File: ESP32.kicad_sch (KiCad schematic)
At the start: 20 parts, among them J1 USB_B_Micro, SW1 Boot, SW2 Reset, U3 ESP32-S3-MINI-1, U4 USBLC6-2SC6

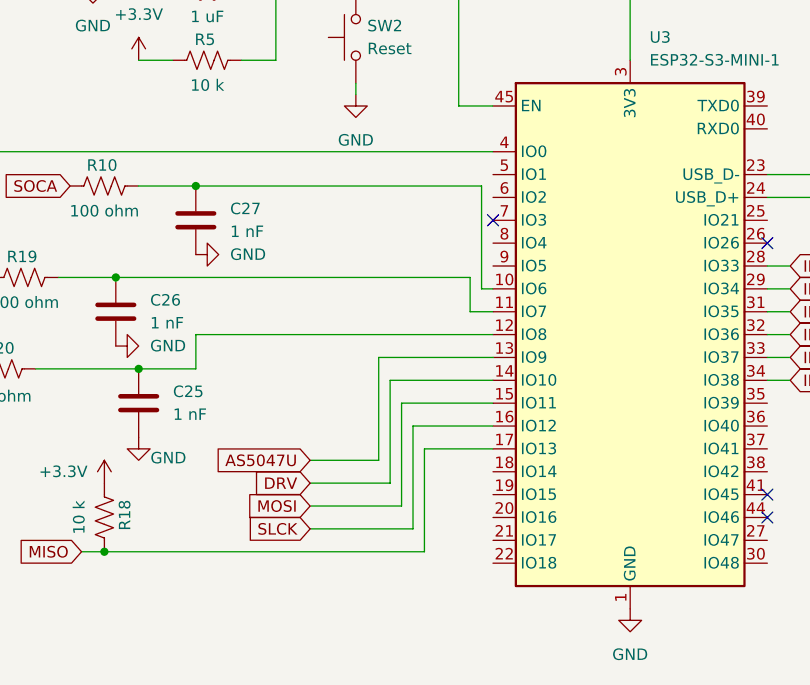
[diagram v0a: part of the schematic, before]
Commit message: Added additional Labels
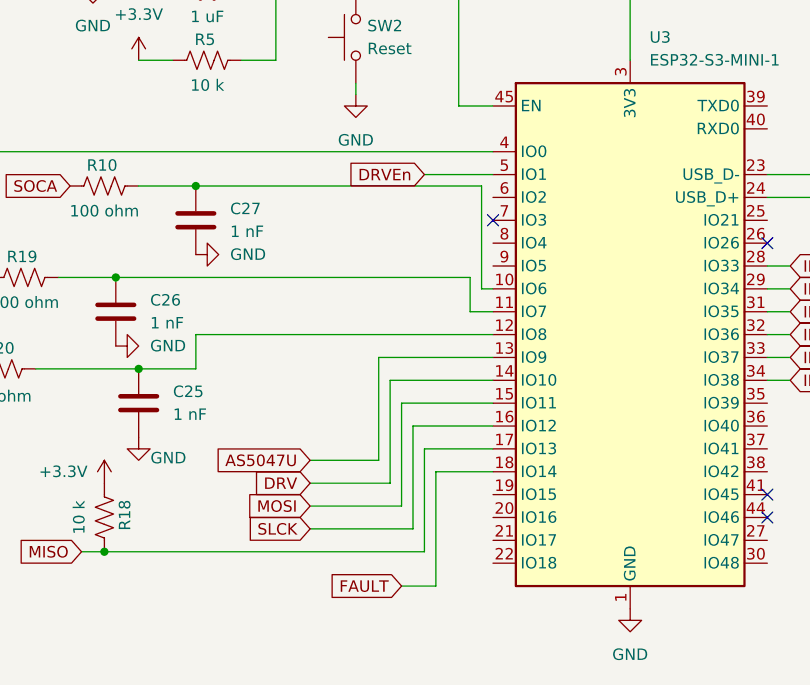
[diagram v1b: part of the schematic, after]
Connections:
- net FAULT: now reaches U3.18 (IO14)
- net DRVEn: now reaches U3.5 (IO1)
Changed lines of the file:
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@@
+	(wire
+		(pts
+			(xy 123.19 78.74) (xy 130.81 78.74)
+		)
+		(stroke
+			(width 0)
+			(type default)
+		)
+	)
 	(wire
 		(pts
@@
 	(wire
 		(pts
+			(xy 124.46 124.46) (xy 124.46 111.76)
+		)
+		(stroke
+			(width 0)
+			(type default)
+		)
+	)
+	(wire
+		(pts
 			(xy 118.11 110.49) (xy 118.11 99.06)
 		)
@@
 	(wire
 		(pts
+			(xy 124.46 111.76) (xy 130.81 111.76)
+		)
+		(stroke
+			(width 0)
+			(type default)
+		)
+	)
+	(wire
+		(pts
 			(xy 161.29 78.74) (xy 212.09 78.74)
 		)
@@
 	(wire
 		(pts
+			(xy 120.65 124.46) (xy 124.46 124.46)
+		)
+		(stroke
+			(width 0)
+			(type default)
+		)
+	)
+	(wire
+		(pts
 			(xy 106.68 57.15) (xy 106.68 58.42)
 		)
@@
 		)
 	)
+	(global_label "DRVEn"
+		(shape input)
+		(at 123.19 78.74 180)
+		(fields_autoplaced yes)
+		(effects
+			(font
+				(size 1.27 1.27)
+			)
+			(justify right)
+		)
+		(property "Intersheetrefs" "${INTERSHEET_REFS}"
+			(at 114.2782 78.74 0)
+			(effects
+				(font
+					(size 1.27 1.27)
+				)
+				(justify right)
+				(hide yes)
+			)
+		)
+	)
 	(global_label "MOSI"
 		(shape input)
@@
 			(effects
 				(font
+					(size 1.27 1.27)
+				)
+				(justify right)
+				(hide yes)
+			)
+		)
+	)
+	(global_label "FAULT"
+		(shape input)
+		(at 120.65 124.46 180)
+		(fields_autoplaced yes)
+		(effects
+			(font
+				(size 1.27 1.27)
+			)
+			(justify right)
+		)
+		(property "Intersheetrefs" "${INTERSHEET_REFS}"
+			(at 112.1614 124.46 0)
+			(effects
+				(font

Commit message: Layed out PCB
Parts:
- C10: footprint (none) -> Capacitor_SMD:C_0603_1608Metric
- C11, C24, C25, C26, C27, C8, C9: footprint (none) -> Capacitor_SMD:C_0402_1005Metric
- R10, R18, R19, R20, R5, R6: footprint (none) -> Resistor_SMD:R_0603_1608Metric
- SW1, SW2: footprint (none) -> SMD_Button:SW_3x6_SMD_LCSC
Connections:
- net SOCA: now also R20.1; no longer R10.1
- net SOCC: now also R10.1; no longer R20.1
- net D-: now reaches U3.23 (USB_D-), U4.4 (I/O2)
- net D-: now also J1.2 (D-), U4.3 (I/O2)
- net D+: now reaches U3.24 (USB_D+), U4.6 (I/O1)
- net D+: now also J1.3 (D+), U4.1 (I/O1)
- no-connect marks 5 -> 21
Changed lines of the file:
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@@
 	)
 	(no_connect
+		(at 161.29 121.92)
+	)
+	(no_connect
+		(at 130.81 121.92)
+	)
+	(no_connect
+		(at 130.81 81.28)
+	)
+	(no_connect
+		(at 130.81 116.84)
+	)
+	(no_connect
 		(at 161.29 116.84)
 	)
 	(no_connect
+		(at 130.81 86.36)
+	)
+	(no_connect
 		(at 161.29 86.36)
 	)
 	(no_connect
+		(at 161.29 71.12)
+	)
+	(no_connect
+		(at 161.29 109.22)
+	)
+	(no_connect
+		(at 130.81 88.9)
+	)
+	(no_connect
 		(at 233.68 76.2)
 	)
 	(no_connect
+		(at 161.29 73.66)
+	)
+	(no_connect
+		(at 161.29 106.68)
+	)
+	(no_connect
 		(at 130.81 83.82)
 	)
 	(no_connect
+		(at 161.29 83.82)
+	)
+	(no_connect
+		(at 161.29 119.38)
+	)
+	(no_connect
+		(at 130.81 114.3)
+	)
+	(no_connect
+		(at 161.29 104.14)
+	)
+	(no_connect
 		(at 161.29 114.3)
 	)
+	(no_connect
+		(at 130.81 119.38)
+	)
+	(no_connect
+		(at 161.29 111.76)
+	)
 	(wire
 		(pts
@@
 	(wire
 		(pts
+			(xy 109.22 85.09) (xy 109.22 80.01)
+		)
+		(stroke
+			(width 0)
+			(type default)
+		)
+	)
+	(wire
+		(pts
+			(xy 97.79 80.01) (xy 109.22 80.01)
+		)
+		(stroke
+			(width 0)
+			(type default)
+		)
+	)
+	(wire
+		(pts
 			(xy 161.29 96.52) (xy 163.83 96.52)
 		)
@@
 	(wire
 		(pts
+			(xy 129.54 85.09) (xy 109.22 85.09)
+		)
+		(stroke
+			(width 0)
+			(type default)
+		)
+	)
+	(wire
+		(pts
 			(xy 236.22 100.33) (xy 231.14 100.33)
 		)
@@
 	(wire
 		(pts
-			(xy 129.54 80.01) (xy 129.54 91.44)
-		)
-		(stroke
-			(width 0)
-			(type default)
-		)
-	)
-	(wire
-		(pts
 			(xy 63.5 76.2) (xy 130.81 76.2)
 		)
@@
 	(wire
 		(pts
-			(xy 97.79 80.01) (xy 129.54 80.01)
-		)
-		(stroke
-			(width 0)
-			(type default)
-		)
-	)
-	(wire
-		(pts
 			(xy 233.68 81.28) (xy 222.25 81.28)
 		)
@@
 	(wire
 		(pts
+			(xy 97.79 81.28) (xy 97.79 80.01)
+		)
+		(stroke
+			(width 0)
+			(type default)
+		)
+	)
+	(wire
+		(pts
 			(xy 214.63 90.17) (xy 217.17 90.17)
 		)
@@
 	(wire
 		(pts
+			(xy 129.54 91.44) (xy 129.54 85.09)
+		)
+		(stroke
+			(width 0)
+			(type default)
+		)
+	)
+	(wire
+		(pts
 			(xy 250.19 68.58) (xy 243.84 68.58)
 		)
@@
 		)
 	)
-	(global_label "SOCA"
-		(shape input)
-		(at 83.82 80.01 180)
-		(fields_autoplaced yes)
+	(label "D+"
+		(at 165.1 81.28 0)
 		(effects
 			(font
 				(size 1.27 1.27)
 			)
-			(justify right)
+			(justify left bottom)
 		)
-		(property "Intersheetrefs" "${INTERSHEET_REFS}"
-			(at 75.9362 80.01 0)
-			(effects
-				(font
-					(size 1.27 1.27)
-				)
-				(justify right)
-				(hide yes)
+	)
+	(label "D-"
+		(at 227.33 78.74 0)
+		(effects
+			(font
+				(size 1.27 1.27)
+			)
+			(justify left bottom)
+		)
+	)
+	(label "D+"
+		(at 227.33 81.28 0)
+		(effects
+			(font
+				(size 1.27 1.27)
+			)
+			(justify left bottom)
+		)
+	)
+	(label "D-"
+		(at 165.1 78.74 0)
+		(effects
+			(font
+				(size 1.27 1.27)
 			)
+			(justify left bottom)
 		)
 	)
@@
 		)
 	)
+	(global_label "SOCC"
+		(shape input)
+		(at 83.82 80.01 180)
+		(fields_autoplaced yes)
+		(effects
+			(font
+				(size 1.27 1.27)
+			)
+			(justify right)
+		)
+		(property "Intersheetrefs" "${INTERSHEET_REFS}"
+			(at 75.7548 80.01 0)
+			(effects
+				(font
+					(size 1.27 1.27)
+				)
+				(justify right)
+				(hide yes)
+			)
+		)
+	)
 	(global_label "SOCB"
 		(shape input)
@@
 		)
 	)
-	(global_label "MOSI"
+	(global_label "SOCA"
 		(shape input)
-		(at 110.49 115.57 180)
+		(at 71.12 100.33 180)
 		(fields_autoplaced yes)
 		(effects
@@
 		)
 		(property "Intersheetrefs" "${INTERSHEET_REFS}"
-			(at 102.9086 115.57 0)
+			(at 63.2362 100.33 0)
 			(effects
 				(font
@@
 		)
 	)
-	(global_label "AS5047U"
+	(global_label "MOSI"
 		(shape input)
-		(at 110.49 110.49 180)
+		(at 110.49 115.57 180)
 		(fields_autoplaced yes)
 		(effects
@@
 		)
 		(property "Intersheetrefs" "${INTERSHEET_REFS}"
-			(at 99.0382 110.49 0)
+			(at 102.9086 115.57 0)
 			(effects
 				(font
@@
 		)
 	)
-	(global_label "INLC"
+	(global_label "AS5047U"
 		(shape input)
-		(at 163.83 101.6 0)
+		(at 110.49 110.49 180)
 		(fields_autoplaced yes)
 		(effects
@@
 				(size 1.27 1.27)
 			)
-			(justify left)
+			(justify right)
 		)
 		(property "Intersheetrefs" "${INTERSHEET_REFS}"
-			(at 171.0486 101.6 0)
+			(at 99.0382 110.49 0)
 			(effects
 				(font
 					(size 1.27 1.27)
 				)
-				(justify left)
+				(justify right)
 				(hide yes)
 			)
 		)
 	)
-	(global_label "SOCC"
+	(global_label "INLC"
 		(shape input)
-		(at 71.12 100.33 180)
+		(at 163.83 101.6 0)
 		(fields_autoplaced yes)
 		(effects
@@
 				(size 1.27 1.27)
 			)
-			(justify right)
+			(justify left)
 		)
 		(property "Intersheetrefs" "${INTERSHEET_REFS}"
-			(at 63.0548 100.33 0)
+			(at 171.0486 101.6 0)
 			(effects
 				(font
 					(size 1.27 1.27)
 				)
-				(justify right)
+				(justify left)
 				(hide yes)
 			)
@@
 			)
 		)
-		(property "Footprint" ""
+		(property "Footprint" "Capacitor_SMD:C_0603_1608Metric"
 			(at 127.9652 50.8 0)
 			(effects
@@
 			)
 		)
-		(property "Footprint" ""
+		(property "Footprint" "Resistor_SMD:R_0603_1608Metric"
 			(at 88.646 117.094 90)
 			(effects
@@
 			)
 		)
-		(property "Footprint" ""
+		(property "Footprint" "Resistor_SMD:R_0603_1608Metric"
 			(at 78.994 89.154 90)
 			(effects
@@
 			)
 		)
-		(property "Footprint" ""
+		(property "Footprint" "Resistor_SMD:R_0603_1608Metric"
 			(at 87.884 78.994 90)
 			(effects
@@
 			)
 		)
-		(property "Footprint" ""
+		(property "Footprint" "Capacitor_SMD:C_0402_1005Metric"
 			(at 92.4052 107.95 0)
 			(effects
@@
 			)
 		)
-		(property "Footprint" ""
+		(property "Footprint" "Capacitor_SMD:C_0402_1005Metric"
 			(at 214.63 89.2048 0)
 			(effects
@@
 			)
 		)
-		(property "Footprint" ""
+		(property "Footprint" "Resistor_SMD:R_0603_1608Metric"
 			(at 54.864 75.184 90)
 			(effects
@@
 			)
 		)
-		(property "Footprint" ""
+		(property "Footprint" "Capacitor_SMD:C_0402_1005Metric"
 			(at 136.1948 43.18 0)
 			(effects
@@
 			)
 		)
-		(property "Footprint" ""
+		(property "Footprint" "Resistor_SMD:R_0603_1608Metric"
 			(at 99.314 65.024 90)
 			(effects
@@
 			)
 		)
-		(property "Footprint" ""
+		(property "Footprint" "Capacitor_SMD:C_0402_1005Metric"
 			(at 102.87 56.1848 0)
 			(effects
@@
 			)
 		)
-		(property "Footprint" ""
+		(property "Footprint" "SMD_Button:SW_3x6_SMD_LCSC"
 			(at 58.42 81.28 0)
 			(effects
@@
 			)
 		)
-		(property "Footprint" ""
+		(property "Footprint" "Capacitor_SMD:C_0402_1005Metric"
 			(at 89.8652 97.79 0)
 			(effects
@@
 			)
 		)
-		(property "Footprint" ""
+		(property "Footprint" "Capacitor_SMD:C_0402_1005Metric"
 			(at 206.7052 125.73 0)
 			(effects
@@
 			)
 		)
-		(property "Footprint" ""
+		(property "Footprint" "Resistor_SMD:R_0603_1608Metric"
 			(at 76.454 99.314 90)
 			(effects
@@
 			)
 		)
-		(property "Footprint" ""
+		(property "Footprint" "Capacitor_SMD:C_0402_1005Metric"
 			(at 98.7552 87.63 0)
 			(effects
@@
 			)
 		)
-		(property "Footprint" ""
+		(property "Footprint" "SMD_Button:SW_3x6_SMD_LCSC"
 			(at 110.49 63.5 0)
 			(effects

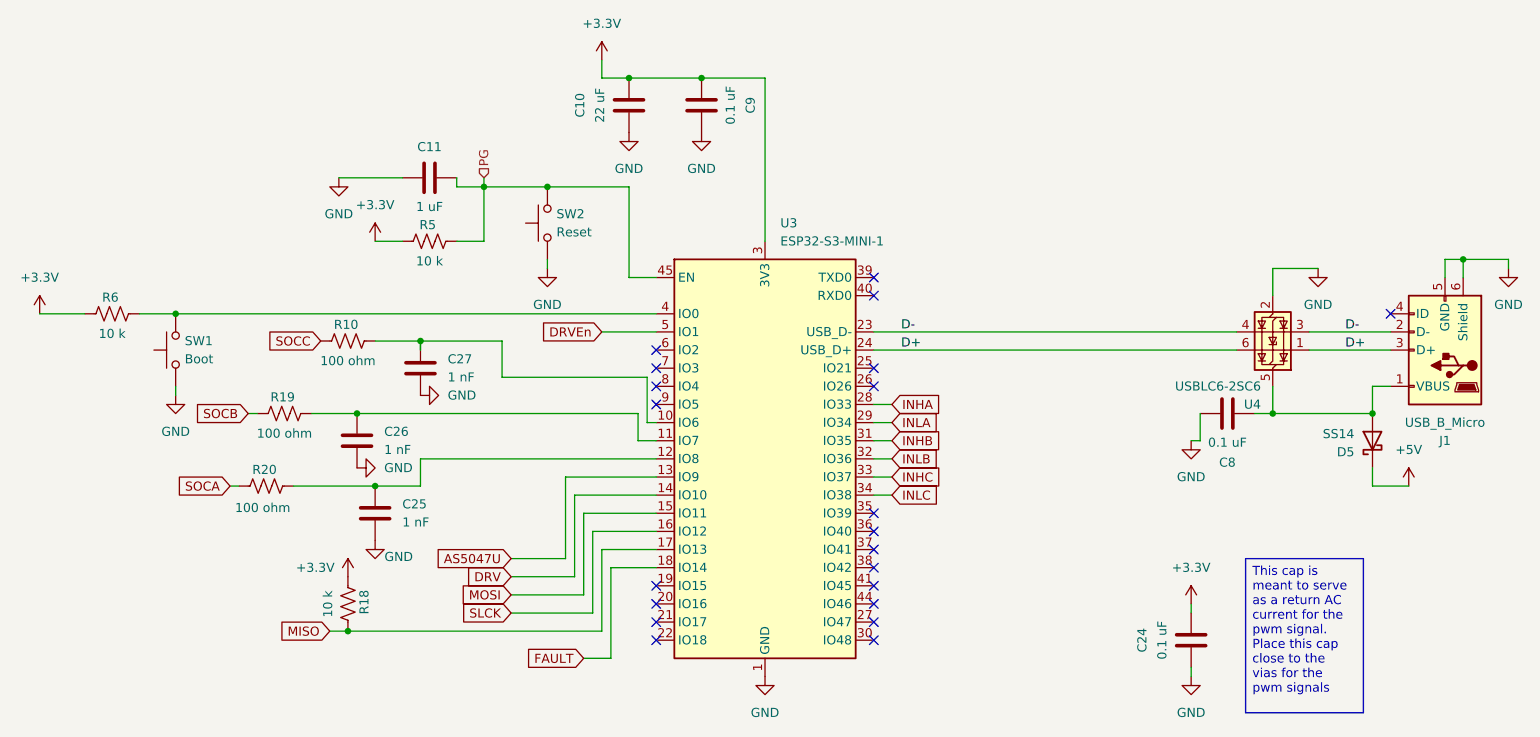
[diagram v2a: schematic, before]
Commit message: finalizing PCB Layouts and traces
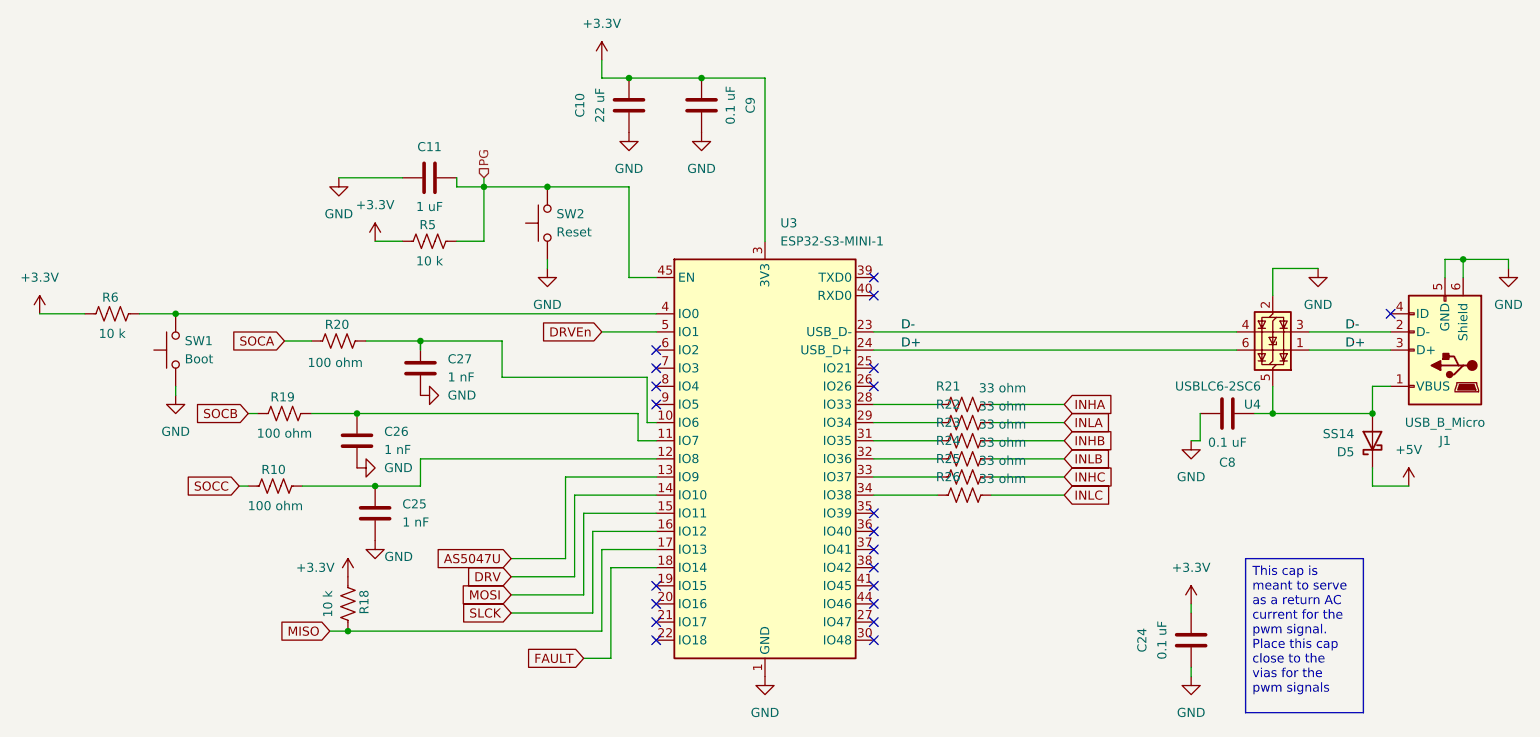
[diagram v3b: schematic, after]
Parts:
- added R21, R22, R23, R24, R25, R26: 33 ohm, Resistor_SMD:R_0402_1005Metric, symbol Device:R_US
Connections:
- net INHA: now also R21.2; no longer U3.28 (IO33)
- net INHB: now also R23.2; no longer U3.31 (IO35)
- net INHC: now also R25.2; no longer U3.33 (IO37)
- net INLA: now also R22.2; no longer U3.29 (IO34)
- net INLB: now also R24.2; no longer U3.32 (IO36)
- net INLC: now also R26.2; no longer U3.34 (IO38)
- net at C27.1, U3.10 (IO6): now also R20.2; no longer R10.2
- net at C25.1, U3.12 (IO8): now also R10.2; no longer R20.2
- new net: R21.1, U3.28 (IO33)
- new net: R22.1, U3.29 (IO34)
- new net: R23.1, U3.31 (IO35)
- new net: R24.1, U3.32 (IO36)
- new net: R25.1, U3.33 (IO37)
- new net: R26.1, U3.34 (IO38)
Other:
- moved on the sheet: R10, R20
